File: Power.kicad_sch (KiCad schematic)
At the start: 31 parts, among them U2 TPS56121, U3 LD1117S33TR_SOT223

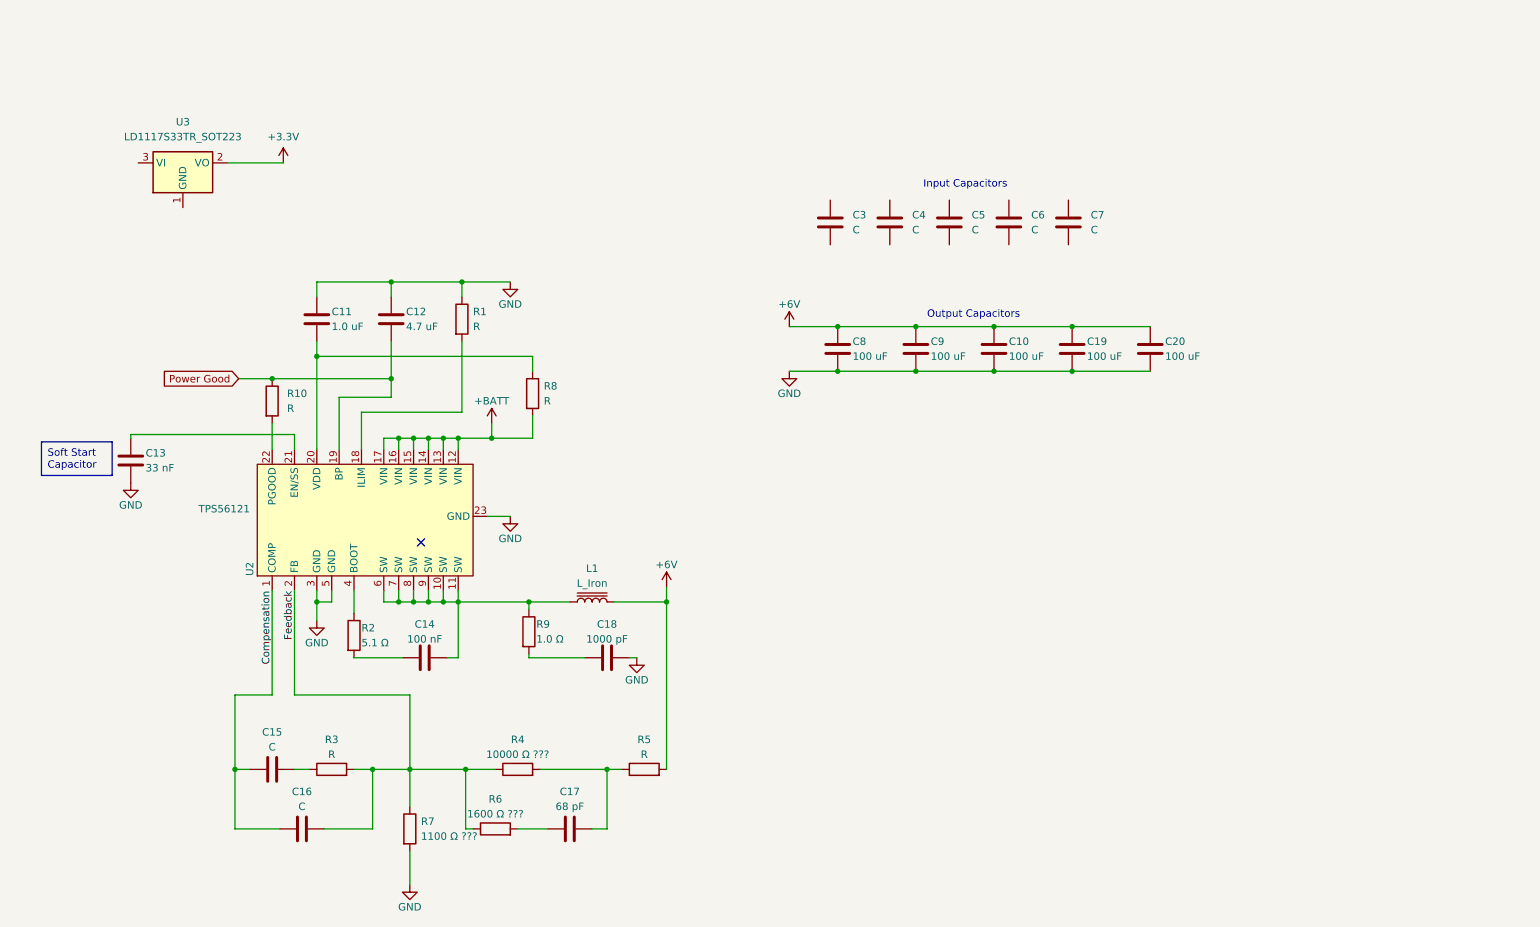
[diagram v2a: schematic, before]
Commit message: Continue buck converter component selection
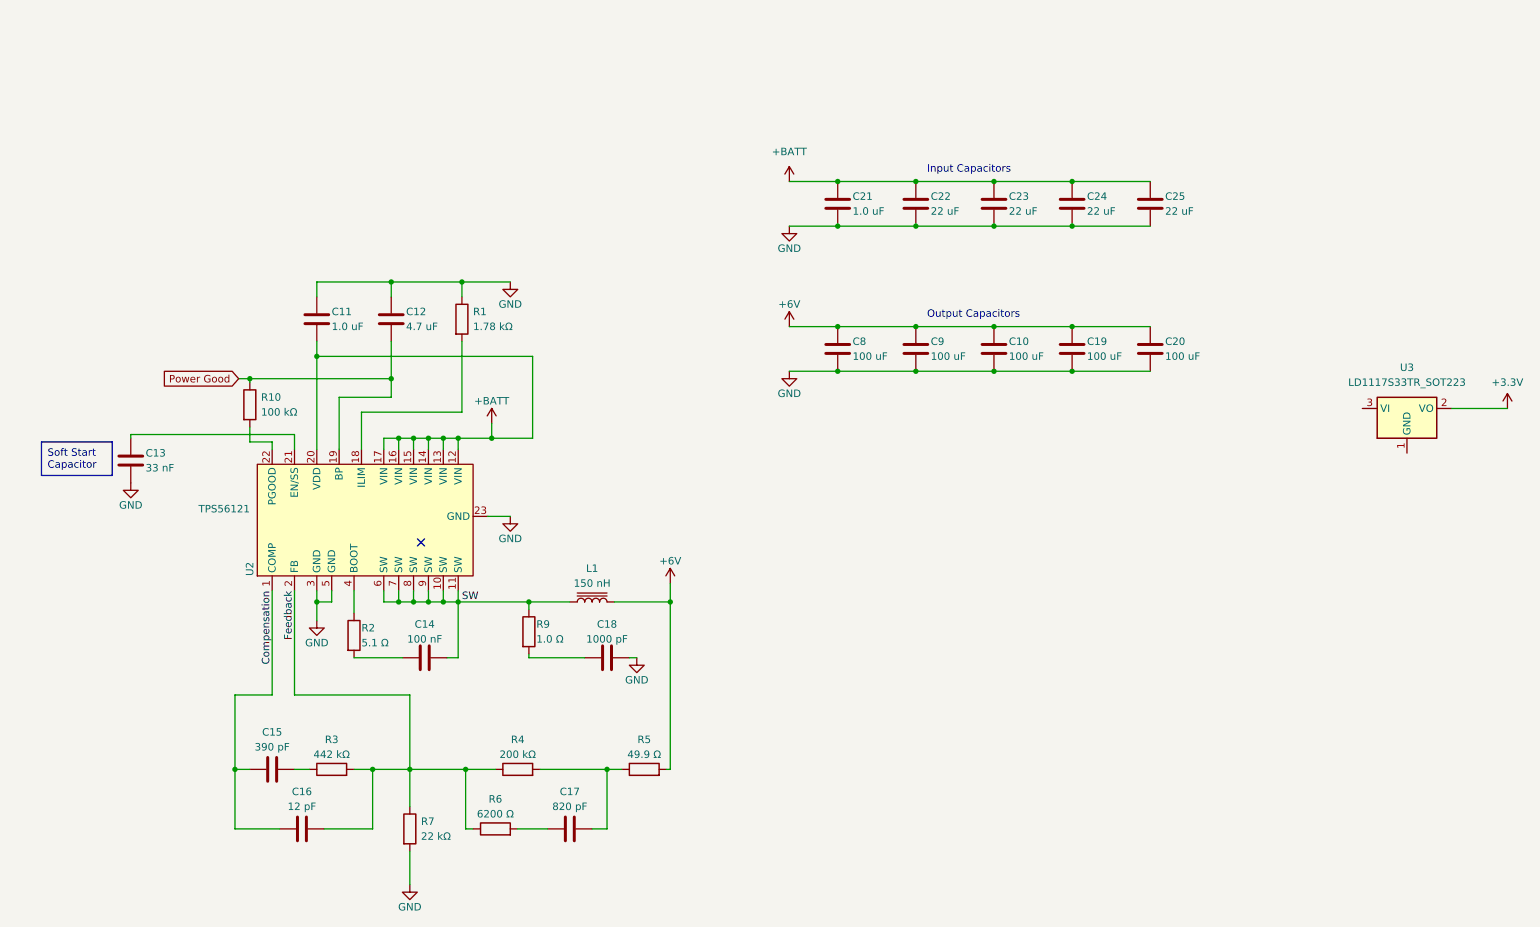
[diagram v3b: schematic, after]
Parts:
- removed C3, C4, C5, C6, C7: C, symbol Device:C
- removed R8: R, symbol Device:R
- added C21: 1.0 uF, Capacitor_SMD:C_1210_3225Metric, symbol Device:C
- added C22, C23, C24, C25: 22 uF, Capacitor_SMD:C_1210_3225Metric, symbol Device:C
- C15: value C -> 390 pF
- C16: value C -> 12 pF
- C17: value 68 pF -> 820 pF
- L1: value L_Iron -> 150 nH; footprint (none) -> Inductor_SMD:L_Sumida_CDMC6D28_7.25x6.5mm; Part No. (none) -> 0624CDMCCDS-R15MC
- R1: value R -> 1.78 kΩ; footprint (none) -> Resistor_SMD:R_0805_2012Metric
- R10: value R -> 100 kΩ; footprint (none) -> Resistor_SMD:R_0805_2012Metric
- R2, R9: footprint (none) -> Resistor_SMD:R_0805_2012Metric
- R3: value R -> 442 kΩ; footprint (none) -> Resistor_SMD:R_0805_2012Metric
- R4: value 10000 Ω ??? -> 200 kΩ; footprint (none) -> Resistor_SMD:R_0805_2012Metric
- R5: value R -> 49.9 Ω; footprint (none) -> Resistor_SMD:R_0805_2012Metric
- R6: value 1600 Ω ??? -> 6200 Ω; footprint (none) -> Resistor_SMD:R_0805_2012Metric
- R7: value 1100 Ω ??? -> 22 kΩ; footprint (none) -> Resistor_SMD:R_0805_2012Metric
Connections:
- net +BATT: now also C11.2, U2.20 (VDD), C21.1, C22.1, C23.1, C24.1, C25.1
- net GND: now also C21.2, C22.2, C23.2, C24.2, C25.2
- net SW: now reaches C14.2, L1.1, R9.1, U2.10 (SW), U2.11 (SW), U2.6 (SW), U2.7 (SW), U2.8 (SW), U2.9 (SW)
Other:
- moved on the sheet: R10, U3

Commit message: Lay out the buck converter circuitry
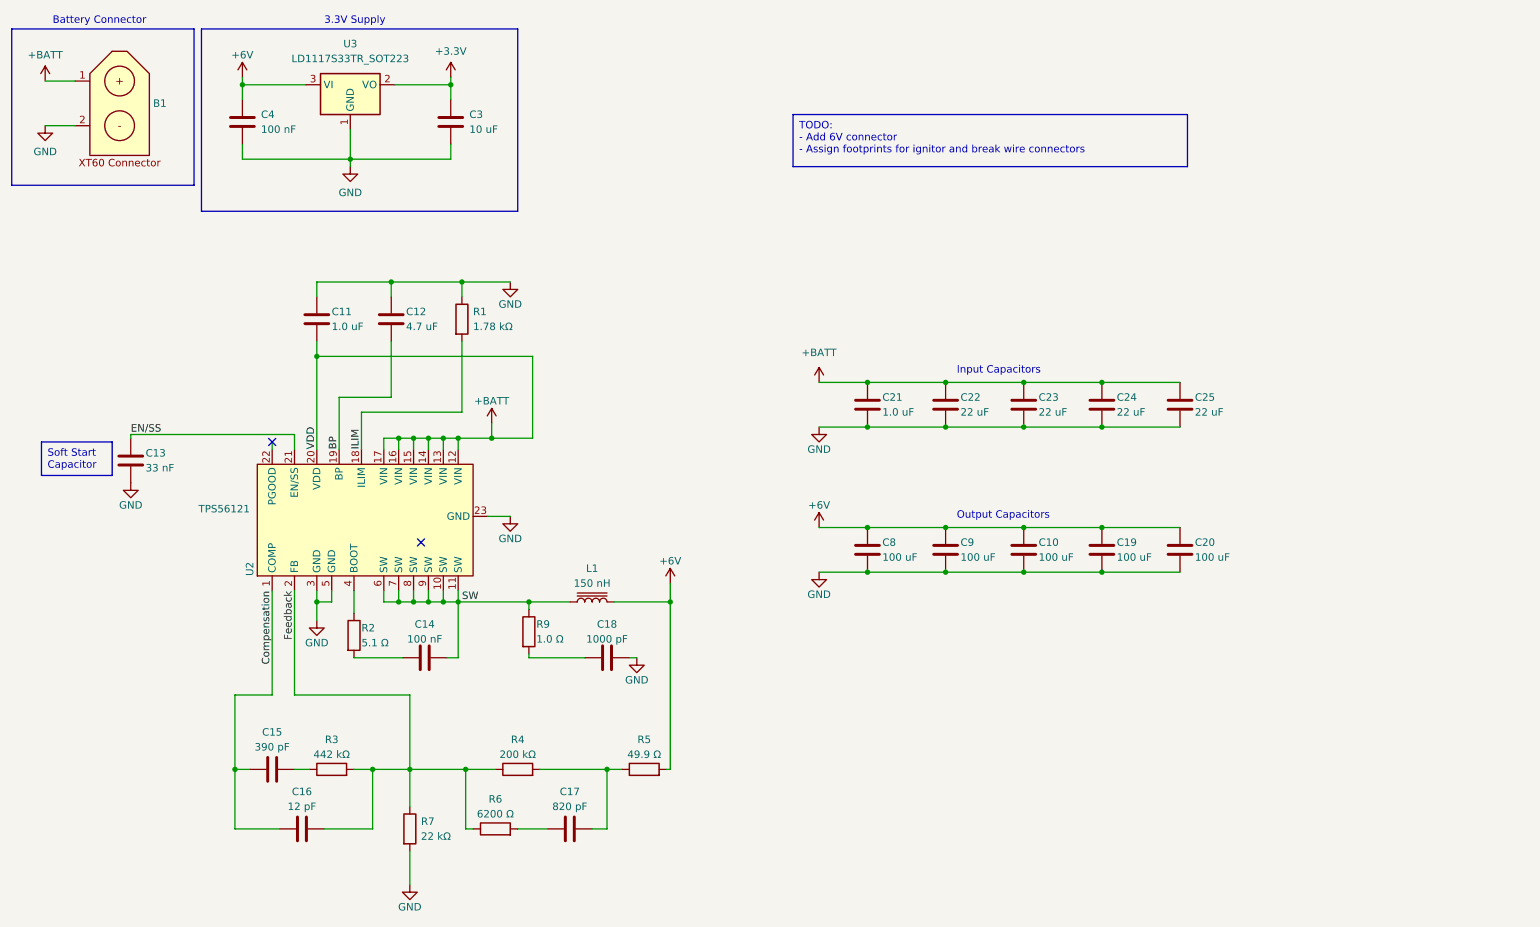
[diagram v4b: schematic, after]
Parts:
- removed R10: 100 kΩ, Resistor_SMD:R_0805_2012Metric, symbol Device:R
- added B1: ~, Connector_AMASS:AMASS_XT60-M_1x02_P7.20mm_Vertical, symbol Marks_Symbols:XT60_Connector_M
- added C3: 10 uF, Capacitor_SMD:C_0805_2012Metric, symbol Device:C
- added C4: 100 nF, Capacitor_SMD:C_0805_2012Metric, symbol Device:C
- C11: footprint (none) -> Capacitor_SMD:C_1210_3225Metric
- C12, C13, C14, C15, C16, C17, C18: footprint (none) -> Capacitor_SMD:C_0805_2012Metric
- C21: Part No. (none) -> CL32B105KBHNNNE
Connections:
- net +3.3V: now also C3.1
- net +6V: now also U3.3 (VI), C4.1
- net +BATT: now also B1.1
- net GND: now also U3.1 (GND), B1.2, C3.2, C4.2
- net EN/SS: now reaches C13.1, U2.21 (EN/SS)
- net ILIM: now reaches R1.2, U2.18 (ILIM)
- net Power Good renamed BP
- no-connect marks 1 -> 2
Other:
- note added: "3.3V Supply"
- note added: "Battery Connector"
- moved on the sheet: C10, C19, C20, C21, C22, C23, C24, C25, C8, C9, U3

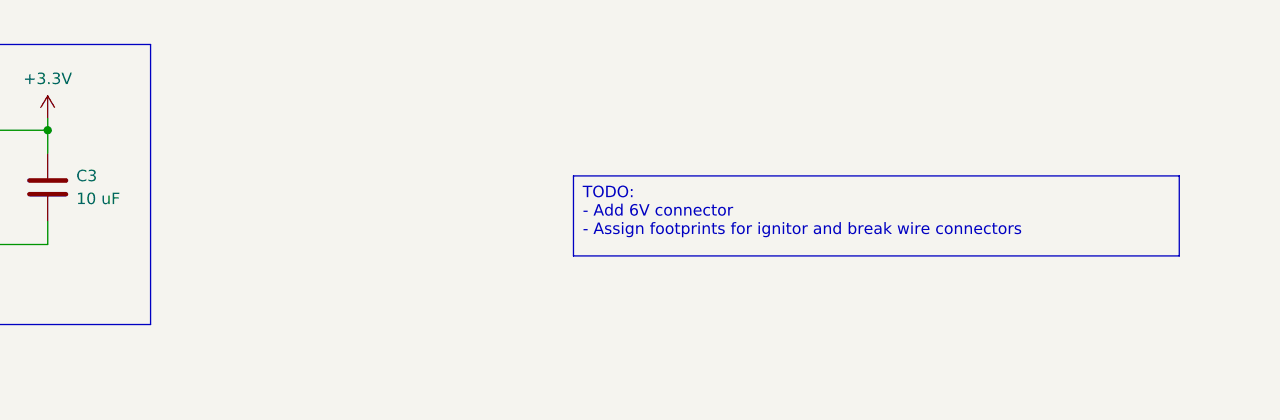
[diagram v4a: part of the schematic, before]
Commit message: Lay out the rest of the components
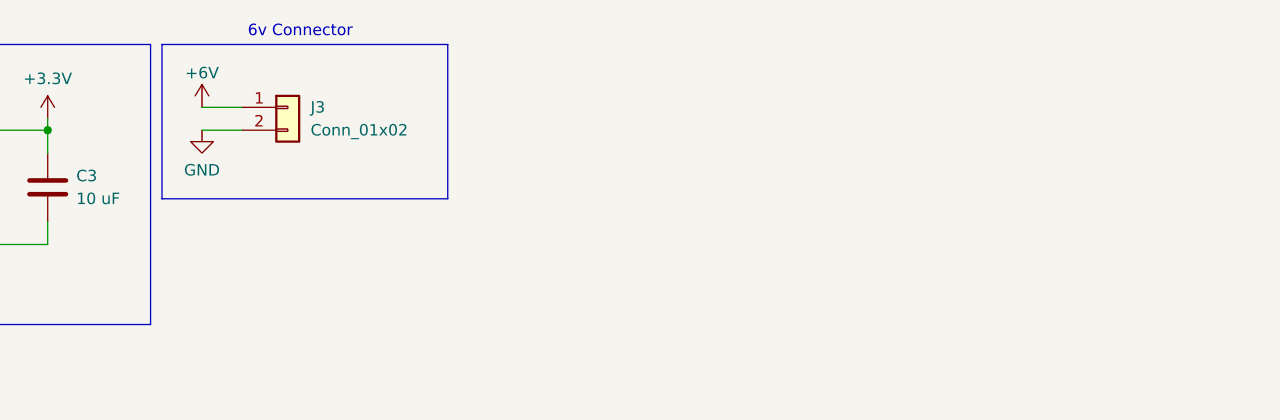
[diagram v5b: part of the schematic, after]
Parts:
- added J3: Conn_01x02, Connector_Wire:SolderWire-2sqmm_1x02_P7.8mm_D2mm_OD3.9mm, symbol Connector_Generic:Conn_01x02
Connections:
- net +6V: now also J3.1 (Pin_1)
- net GND: now also J3.2 (Pin_2)
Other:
- note added: "6v Connector"
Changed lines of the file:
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@@
+    (stroke (width 0) (type default))
+  )
+  (wire (pts (xy 107.315 24.13) (xy 111.76 24.13))
     (stroke (width 0) (type default))
   )
@@
     (stroke (width 0) (type default))
   )
+  (wire (pts (xy 107.315 26.67) (xy 111.76 26.67))
+    (stroke (width 0) (type default))
+  )
   (wire (pts (xy 116.84 143.51) (xy 116.84 153.67))
     (stroke (width 0) (type default))
@@
     (fill (type none))
   )
-  (text_box "TODO:\n - Add 6V connector\n - Assign footprints for ignitor and break wire connectors"
-    (at 148.59 31.75 0) (size 67.31 8.89)
+  (rectangle (start 102.87 17.145) (end 134.62 34.29)
+    (stroke (width 0) (type default))
+    (fill (type none))
+  )
+  (text_box "Soft Start Capacitor"
+    (at 20.32 87.63 0) (size 12.065 5.715)
     (stroke (width 0) (type default))
     (fill (type none))
     (effects (font (size 1.27 1.27)) (justify left top))
   )
-  (text_box "Soft Start Capacitor"
-    (at 20.32 87.63 0) (size 12.065 5.715)
-    (stroke (width 0) (type default))
-    (fill (type none))
-    (effects (font (size 1.27 1.27)) (justify left top))
-  )
   (text "Battery Connector" (at 22.225 16.51 0)
     (effects (font (size 1.27 1.27)) (justify left bottom))
@@
   )
   (text "Output Capacitors" (at 176.53 100.965 0)
+    (effects (font (size 1.27 1.27)) (justify left bottom))
+  )
+  (text "6v Connector" (at 112.395 16.51 0)
     (effects (font (size 1.27 1.27)) (justify left bottom))
   )
@@
         (path "/64949cb2-91a5-46f3-bf79-1f835924a2e1/8e270b19-1a54-479b-8529-2717edbe00b6"
           (reference "#PWR016") (unit 1)
+        )
+      )
+    )
+  )
+  (symbol (lib_id "power:GND") (at 107.315 26.67 0) (unit 1)
+    (in_bom yes) (on_board yes) (dnp no) (fields_autoplaced)
+    (property "Reference" "#PWR034" (at 107.315 33.02 0)
+      (effects (font (size 1.27 1.27)) hide)
+    )
+    (property "Value" "GND" (at 107.315 31.115 0)
+      (effects (font (size 1.27 1.27)))
+    )
+    (property "Footprint" "" (at 107.315 26.67 0)
+      (effects (font (size 1.27 1.27)) hide)
+    )
+    (property "Datasheet" "" (at 107.315 26.67 0)
+      (effects (font (size 1.27 1.27)) hide)
+    )
+    (pin "1")
+    (instances
+      (project "pad-controller"
+        (path "/64949cb2-91a5-46f3-bf79-1f835924a2e1/8e270b19-1a54-479b-8529-2717edbe00b6"
+          (reference "#PWR034") (unit 1)
         )
       )
@@
     )
   )
+  (symbol (lib_id "Connector_Generic:Conn_01x02") (at 116.84 24.13 0) (unit 1)
+    (in_bom yes) (on_board yes) (dnp no) (fields_autoplaced)
+    (property "Reference" "J3" (at 119.38 24.13 0)
+      (effects (font (size 1.27 1.27)) (justify left))
+    )
+    (property "Value" "Conn_01x02" (at 119.38 26.67 0)
+      (effects (font (size 1.27 1.27)) (justify left))
+    )
+    (property "Footprint" "Connector_Wire:SolderWire-2sqmm_1x02_P7.8mm_D2mm_OD3.9mm" (at 116.84 24.13 0)
+      (effects (font (size 1.27 1.27)) hide)
+    )
+    (property "Datasheet" "~" (at 116.84 24.13 0)
+      (effects (font (size 1.27 1.27)) hide)
+    )
+    (property "Description" "" (at 116.84 24.13 0)
+      (effects (font (size 1.27 1.27)) hide)
+    )
+    (pin "1")
+    (pin "2")
+    (instances
+      (project "pad-controller"
+        (path "/64949cb2-91a5-46f3-bf79-1f835924a2e1"
+          (reference "J3") (unit 1)
+        )
+        (path "/64949cb2-91a5-46f3-bf79-1f835924a2e1/8e270b19-1a54-479b-8529-2717edbe00b6"
+          (reference "J4") (unit 1)
+        )
+      )
+    )
+  )
   (symbol (lib_id "Device:C") (at 214.63 81.28 0) (unit 1)
     (in_bom yes) (on_board yes) (dnp no)
@@
         )
       )
+    )
+  )
+  (symbol (lib_id "power:+6V") (at 107.315 24.13 0) (unit 1)
+    (in_bom yes) (on_board yes) (dnp no)
+    (property "Reference" "#PWR033" (at 107.315 27.94 0)
+      (effects (font (size 1.27 1.27)) hide)
+    )
+    (property "Value" "+6V" (at 107.315 20.32 0)
+      (effects (font (size 1.27 1.27)))
+    )
+    (property "Footprint" "" (at 107.315 24.13 0)
+      (effects (font (size 1.27 1.27)) hide)
+    )
+    (property "Datasheet" "" (at 107.315 24.13 0)
+      (effects (font (size 1.27 1.27)) hide)
+    )
+    (pin "1")
+    (instances
+      (project "pad-controller"
+        (path "/64949cb2-91a5-46f3-bf79-1f835924a2e1/8e270b19-1a54-479b-8529-2717edbe00b6"
+          (reference "#PWR033") (unit 1)
+        )
+      )
